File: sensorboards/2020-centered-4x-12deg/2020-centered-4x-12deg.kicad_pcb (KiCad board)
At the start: 2 copper layers, 45.5 x 48 mm, 14 parts, among them J1 Conn_01x10_Male, U1 CNY70, U2 CNY70, U3 CNY70, U4 CNY70

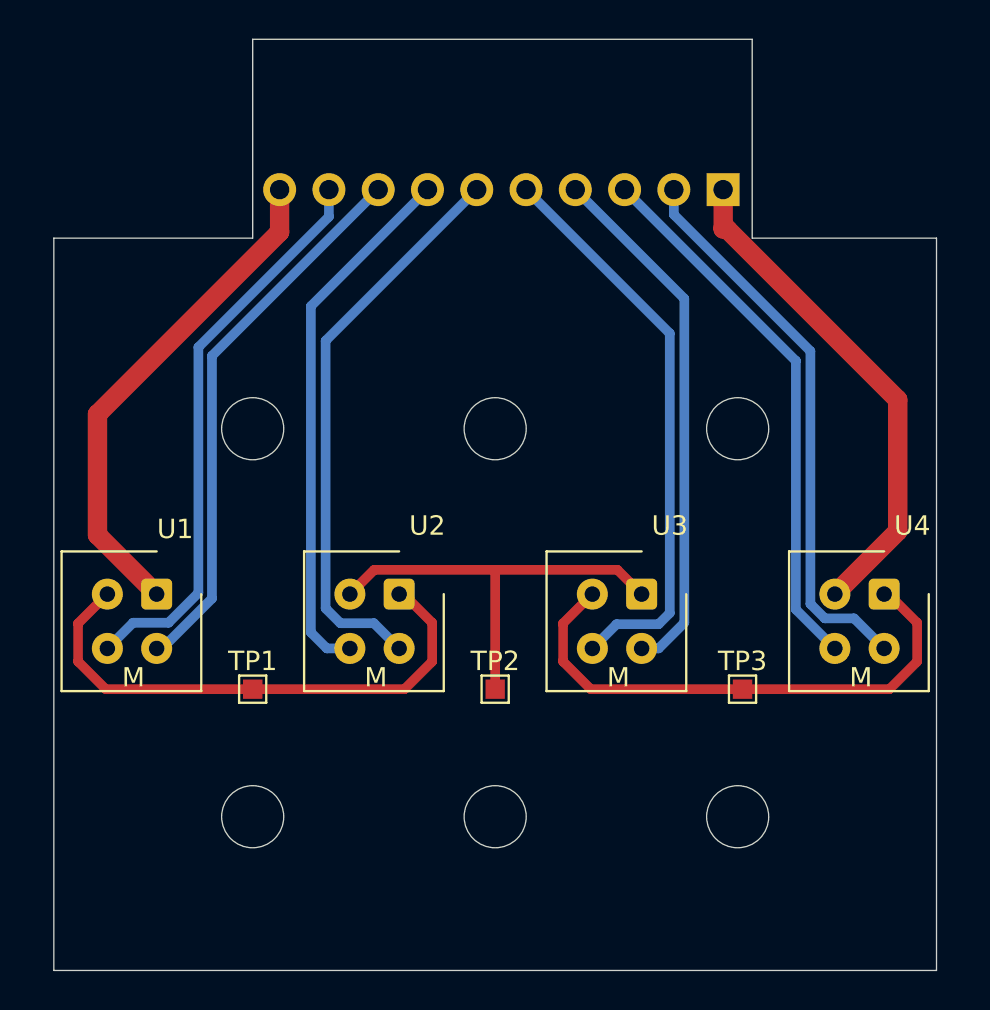
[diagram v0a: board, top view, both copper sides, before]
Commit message: Update 4x boards for issue #44; introduce the 12deg rotated hammer board
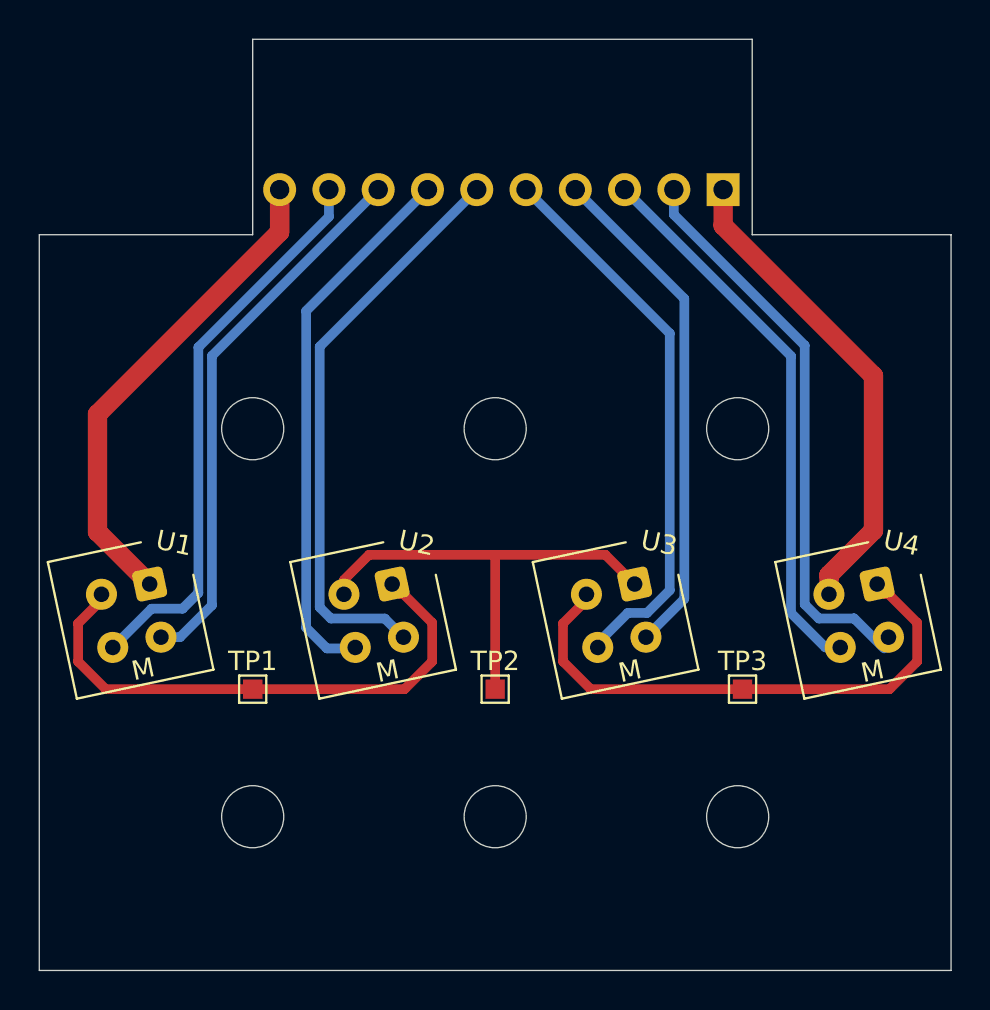
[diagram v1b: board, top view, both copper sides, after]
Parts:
- U1, U2, U3, U4: footprint OptoDevice:Vishay_CNY70 -> footprints:Vishay_CNY70_12DegRotation
- moved U1 1.89 mm to (131.2, 89.8)
- moved U2 1.89 mm to (143.7, 89.8)
- moved U3 1.89 mm to (156.2, 89.8)
- moved U4 1.89 mm to (168.7, 89.8)
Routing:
- net Net-(TP2-Pad1): track 22.3 -> 23.8 mm
- net /E3: track 27.4 -> 26.2 mm
- net /NEG: track 26.0 -> 25.0 mm
- net /C3: track 29.6 -> 29.0 mm
- net /POS: track 26.0 -> 25.3 mm
- net /C4: track 28.1 -> 28.7 mm
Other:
- board size 45.5 x 48 mm -> 47 x 48 mm
